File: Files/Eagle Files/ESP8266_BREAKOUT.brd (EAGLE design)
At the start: 43.2 x 30.5 mm, 17 parts, among them U2 LM1117-3V3-T0-220

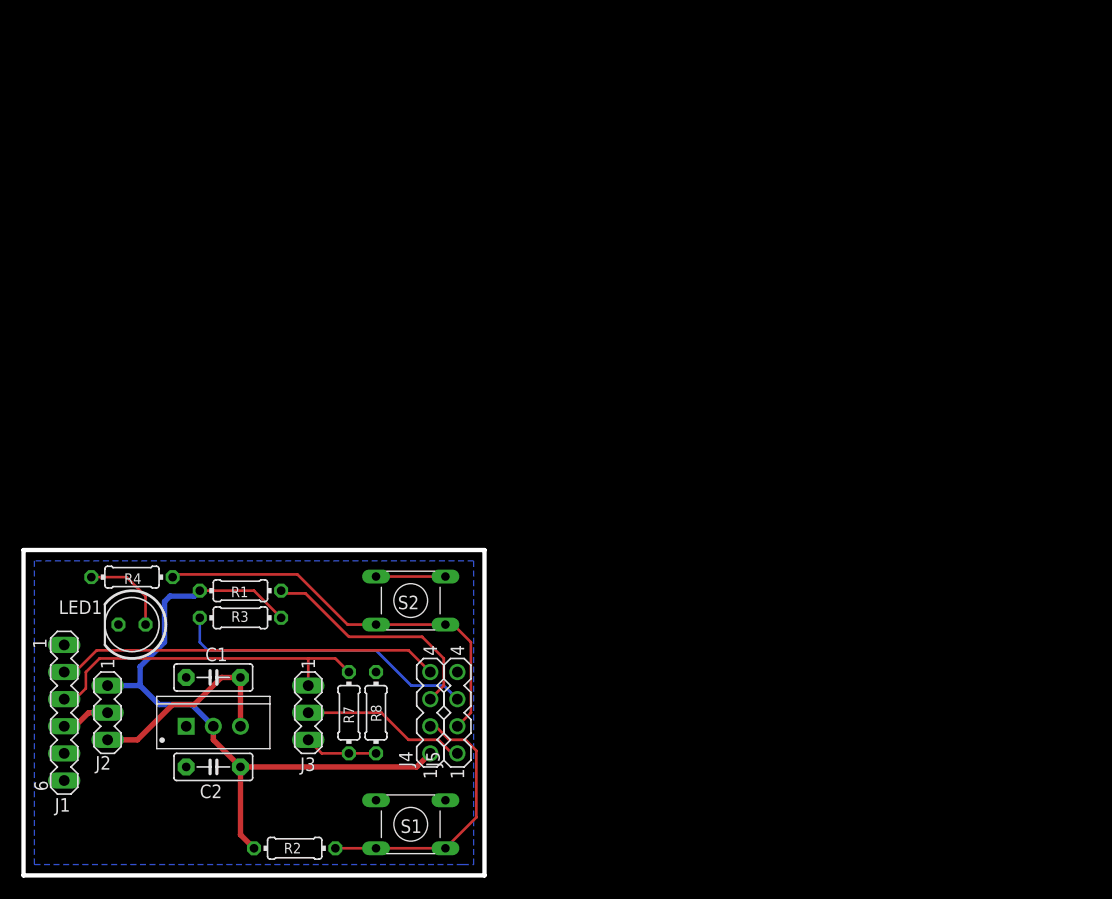
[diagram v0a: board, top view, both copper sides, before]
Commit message: My implementation of the ESP8266-01 breakout board
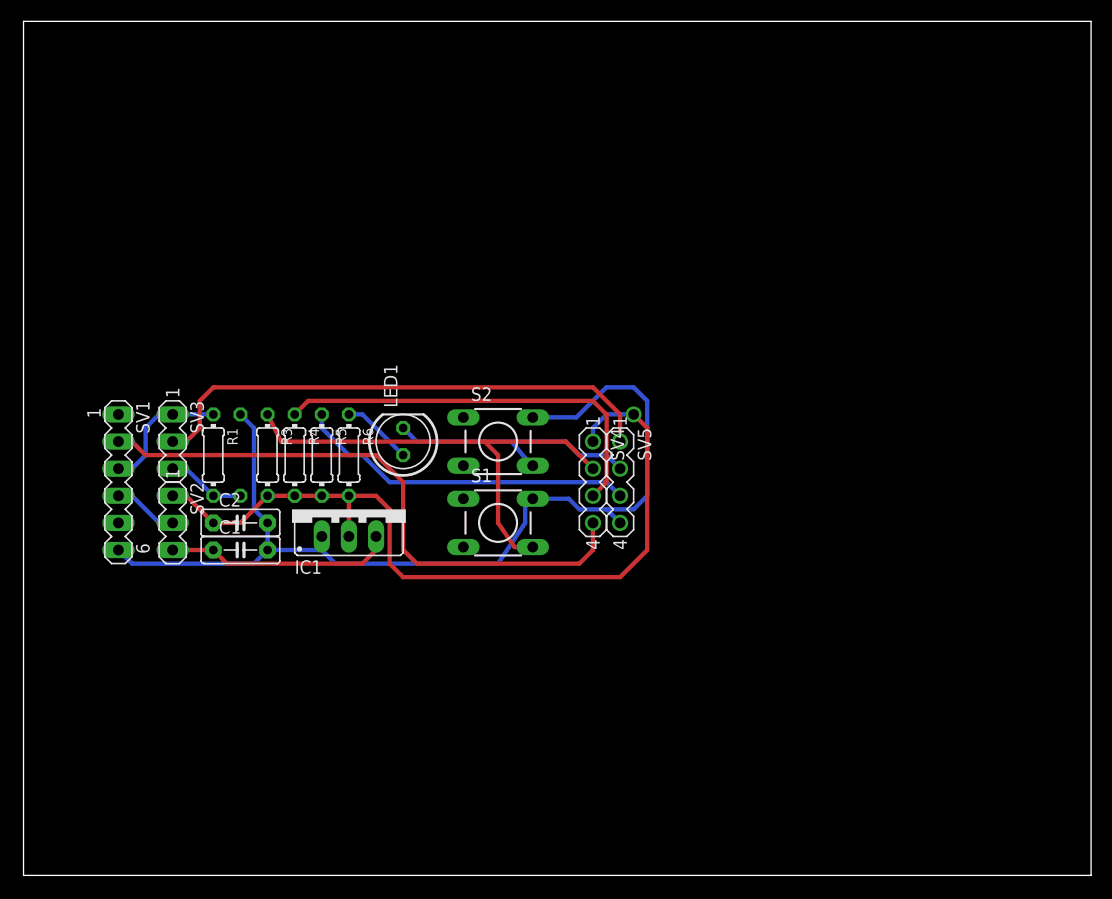
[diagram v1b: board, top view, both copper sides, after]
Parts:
- removed J1: (no value), con-lstb:MA06-1
- removed J2, J3: (no value), con-lstb:MA03-1
- removed J4, J5: (no value), con-lstb:MA04-1
- removed R7: 1K, resistor:0204/7
- removed R8: 1K8, resistor:0204/7
- removed U2: LM1117-3V3-T0-220, LM1117-3V3-TO220:TO-220
- added IC1: 3V3, v-reg:317TS
- added R5: (no value), resistor:0204/7
- added R6: 1K, resistor:0204/7
- added SV1: (no value), con-lstb:MA06-1
- added SV2, SV3: (no value), con-lstb:MA03-1
- added SV4, SV5: (no value), con-lstb:MA04-1
- R1: value 10K -> 1k
- R2: value 10K -> 1K8
- R3: value 10K -> (none)
- R4: value 1K -> (none)
- S1, S2: value 1825910-6-SPST-NOPB-4P -> TACTILE-SWITCH-PTH; device 1825910-6:SW-NOPB-4 -> GeekAmmo:TAC-SWITCH-PTH
- moved R2 37.2 mm to (20.3, 39.4), flipped to the bottom, turned to 90 degrees
- moved S1 32.6 mm to (44.5, 33.0)
- moved LED1 30.6 mm to (35.6, 40.6), turned to 90 degrees
- moved C2 23.0 mm to (20.3, 33.0)
- moved S2 20.6 mm to (44.5, 40.6)
- moved R4 19.0 mm to (25.4, 39.4), turned to 270 degrees
- moved R3 15.5 mm to (22.9, 39.4), turned to 270 degrees
- moved R1 13.0 mm to (17.8, 39.4), turned to 270 degrees
- moved C1 12.2 mm to (20.3, 30.5)
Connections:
- removed net LED: LED1.A, R4.2
- new net N$1: LED1.A, R6.1
- net !RST: now also R3.1, SV4.2; no longer J4.2, R2.2, S1.3
- net +3V3: now also C2.1, IC1.2, R3.2, R4.2, R5.2, R6.2, SV2.1, SV4.1; no longer C2.2, J2.1, J4.1, R1.1, R2.1, R3.1, U2.P$2
- net +5V: now also C1.1, IC1.3, SV2.3; no longer C1.2, J2.3, U2.P$3
- net CH_PD: now also R4.1, SV4.3; no longer J4.3, R1.2
- net GND: now also C1.2, C2.2, IC1.1, R2.2, SV1.6, SV5.4; no longer C1.1, C2.1, J1.6, J5.4, LED1.K, R8.1, S1.1, S2.1, U2.P$1
- net GPIO0: now also LED1.K, SV5.2; no longer J5.2, R4.1, S2.3
- net GPIO2: now also R5.1, SV5.3; no longer J5.3, R3.2
- net RX_PC: now also SV1.2, SV4.4; no longer J1.2, J4.4
- net TX: now also SV3.2, SV5.1; no longer J3.2, J5.1
- net TX_PC: now also R1.1, SV1.3, SV3.1; no longer J1.3, J3.1, R7.2
- net TX_PC_DIV: now also R1.2, R2.1, SV3.3; no longer J3.3, R7.1, R8.2
- net VCC: now also SV1.4, SV2.2; no longer J1.4, J2.2
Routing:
- net GND: track 6.50 -> 94.0 mm
- net TX: track 15.5 -> 49.1 mm
- net RX_PC: track 36.0 -> 56.0 mm
- net !RST: track 25.9 -> 45.7 mm
- net TX_PC: track 32.2 -> 12.5 mm
- net CH_PD: track 22.2 -> 38.4 mm
- net GPIO0: track 39.1 -> 24.9 mm
- net +3V3: track 64.0 -> 76.4 mm, vias 0 -> 1
- net LED: track 8.48 -> 0.00 mm
- net N$1: track 0.00 -> 6.66 mm
- net GPIO2: track 28.6 -> 31.8 mm
- net +5V: track 19.4 -> 21.4 mm
- net VCC: track 4.59 -> 6.13 mm
- net TX_PC_DIV: track 6.88 -> 7.40 mm
- removed copper zone on layer 16, net GND
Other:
- board size 43.2 x 30.5 mm -> 100 x 80 mm
